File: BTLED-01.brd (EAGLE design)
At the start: 85.1 x 57.2 mm, 20 parts

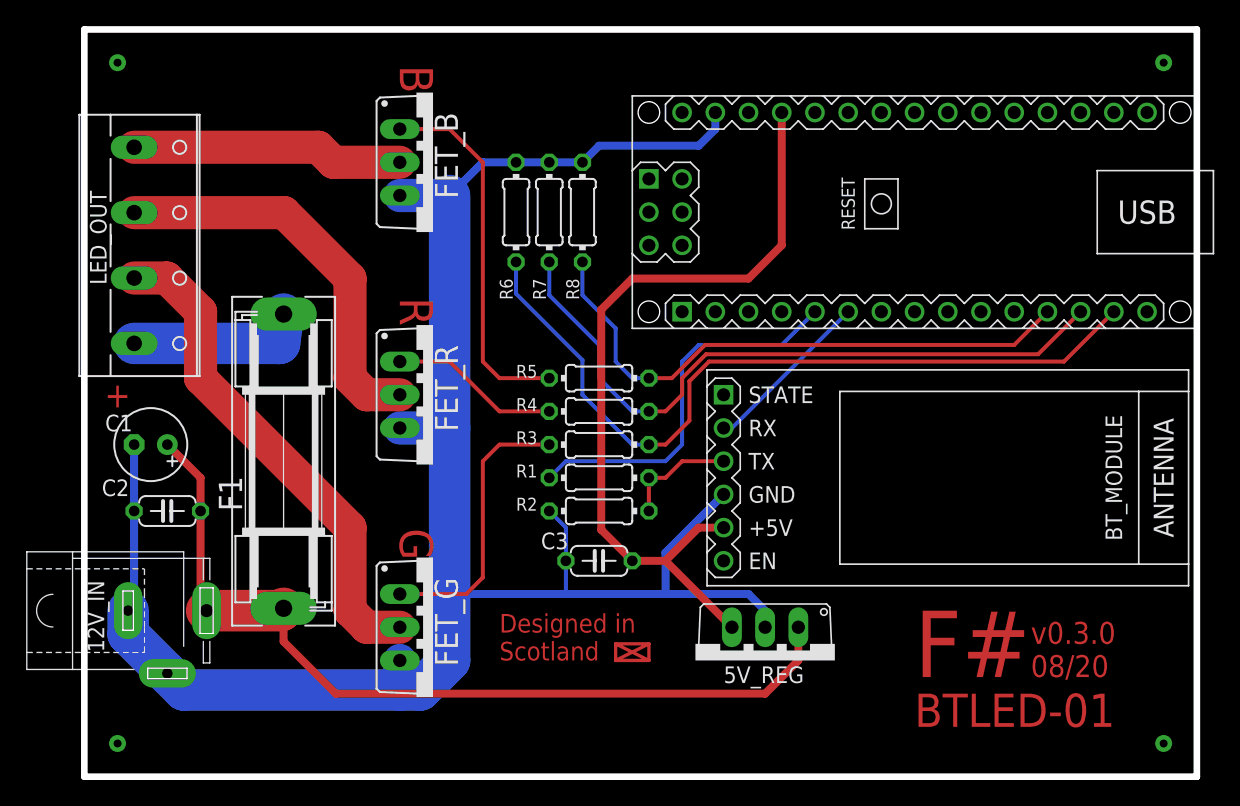
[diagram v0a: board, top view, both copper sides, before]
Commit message: fix: slight tweaks to positioning
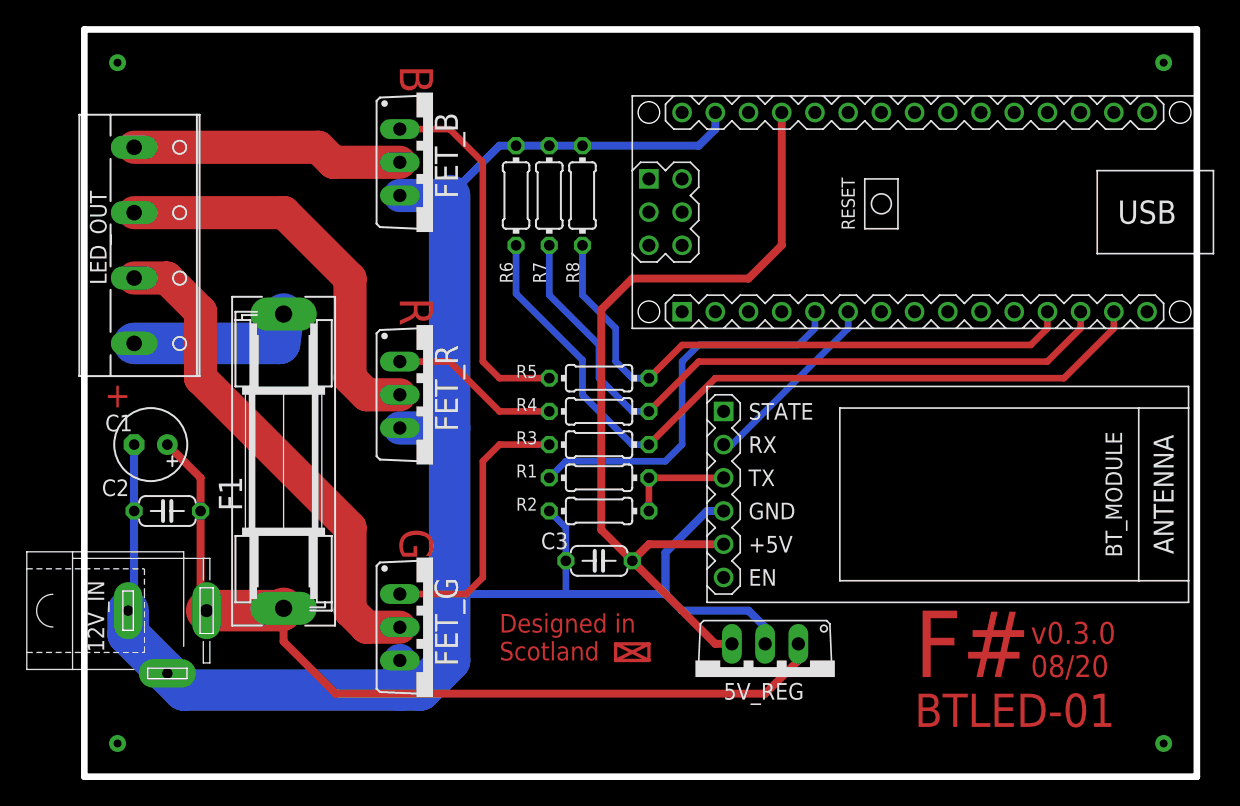
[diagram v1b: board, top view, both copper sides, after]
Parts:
- moved 5V_REG 1.27 mm to (49.5, 35.6)
- moved BT_MODULE 1.27 mm to (63.5, 49.5)
- moved R6 1.27 mm to (30.5, 72.4)
- moved R7 1.27 mm to (33.0, 72.4)
- moved R8 1.27 mm to (35.6, 72.4)
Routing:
- net 5V: track 61.4 -> 64.0 mm
- net B_SIG_1: track 44.3 -> 46.3 mm
- net 12V_IN: track 67.1 -> 65.8 mm
- net R_SIG_1: track 52.3 -> 53.5 mm
- net BT_TX: track 13.2 -> 14.5 mm
- net BT_RX_5V: track 29.3 -> 30.0 mm
- net BT_RX_3.3V: track 8.78 -> 8.25 mm
